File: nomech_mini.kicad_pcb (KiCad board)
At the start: 2 copper layers, 80 x 100 mm, 140 parts, among them CON1 USB_2B, CON2 AVR-ISP-6, P2 CONN_1, P3 CONN_1, P4 CONN_1, P5 CONN_1, P6 CONN_1, Q1 MOSFET_N, Q2 MOSFET_N, Q3 MOSFET_N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

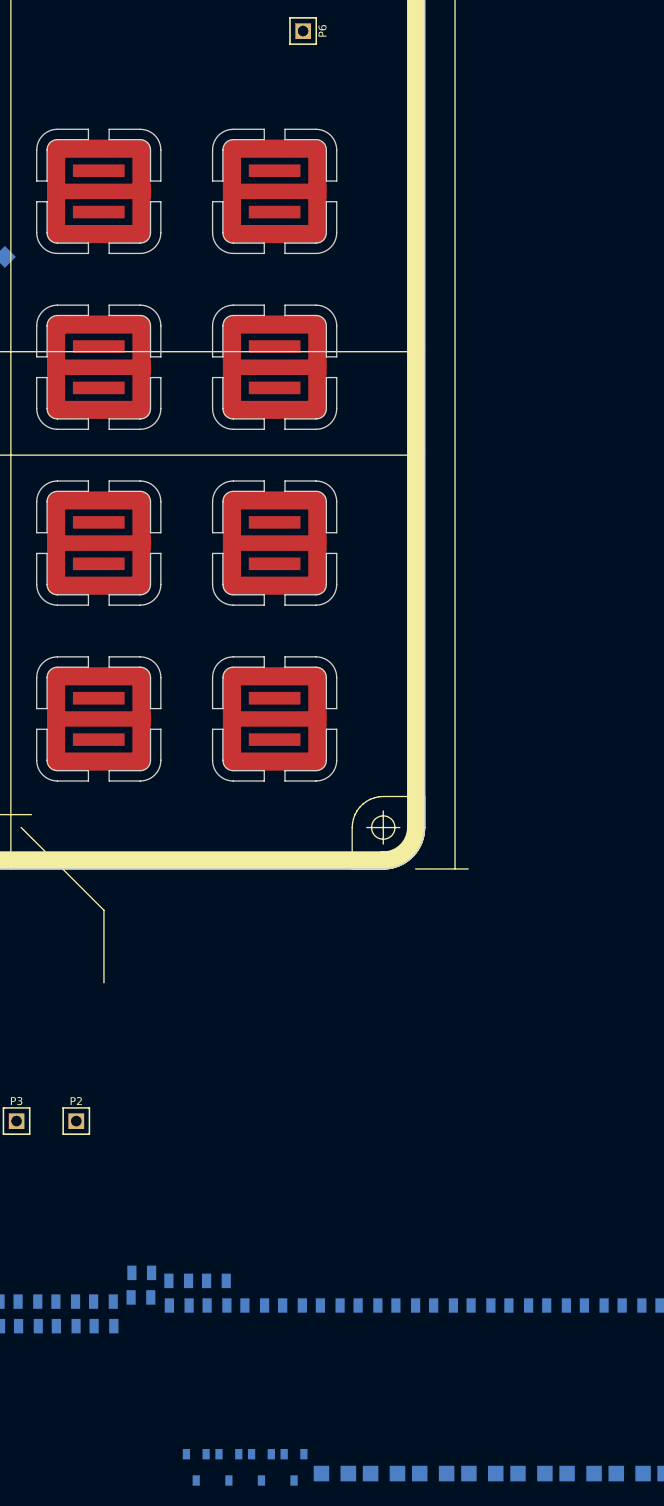
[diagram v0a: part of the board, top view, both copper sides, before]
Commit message: laying out LEDs
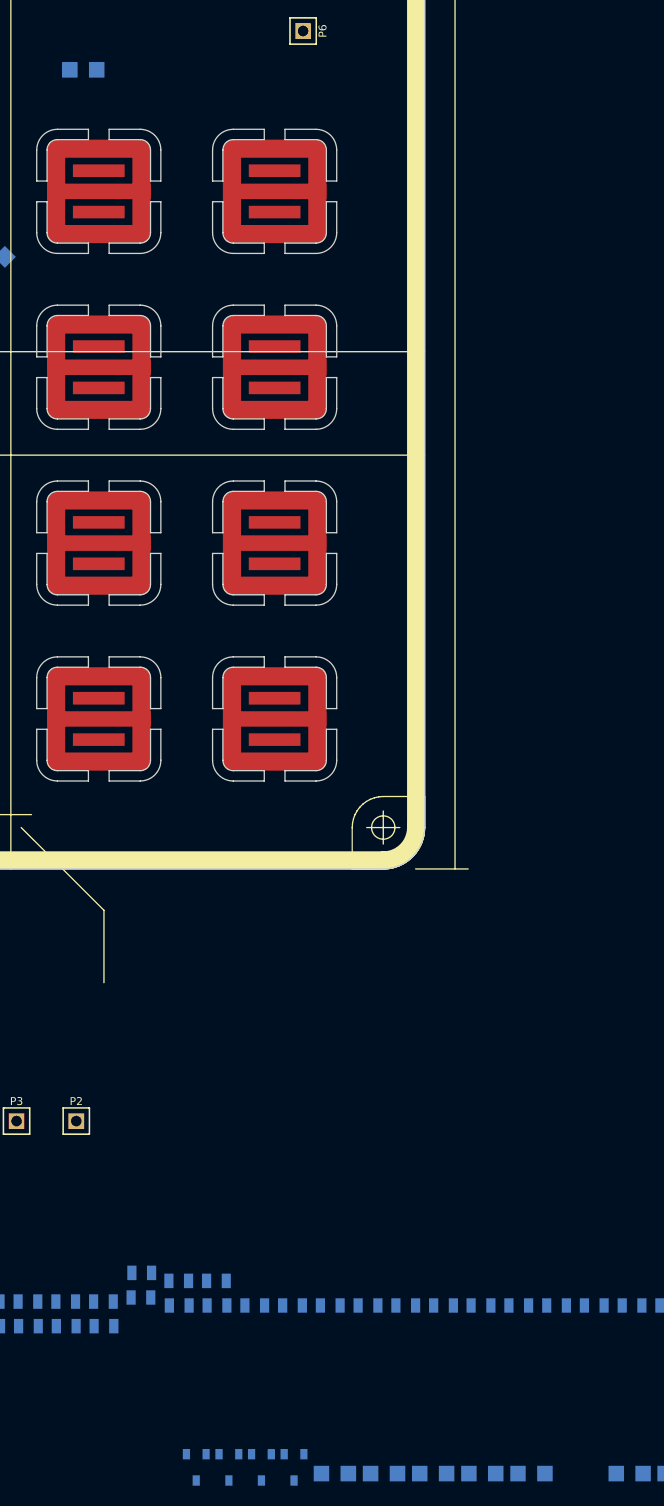
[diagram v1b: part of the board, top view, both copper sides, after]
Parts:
- moved D5 144.0 mm to (146.2, 106.5)
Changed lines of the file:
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@@
   )
   (module KPJA-2107SURCK (layer Back)
-    (at 194.325 242.2)
+    (at 146.25 106.5)
     (attr smd)
     (fp_text reference D5 (at 0.05 1.85) (layer B.SilkS)

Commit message: placing LEDS, working out laser cutting
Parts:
- moved D7 175.8 mm to (157.8, 111.2), turned to 45 degrees
- moved D9 173.1 mm to (106.8, 128.2), turned to 45 degrees
- moved R27 163.2 mm to (122.8, 115.8), turned to 90 degrees
- moved D33 160.8 mm to (147.2, 93.5)
- moved D19 160.2 mm to (123.8, 145.2), turned to 45 degrees
- moved R28 159.4 mm to (133.2, 126.2)
- moved D15 156.8 mm to (157.8, 128.2), turned to 45 degrees
- moved R25 154.8 mm to (105.8, 115.2), turned to 90 degrees
- moved D6 154.7 mm to (154.8, 125.2), turned to 225 degrees
- moved D25 137.0 mm to (106.8, 162.2), turned to 45 degrees
- moved D22 134.6 mm to (154.8, 159.2), turned to 225 degrees
- moved D23 131.5 mm to (157.8, 145.2), turned to 45 degrees
- moved D13 128.0 mm to (140.8, 128.2), turned to 45 degrees
- moved D14 123.7 mm to (154.8, 142.2), turned to 225 degrees
- moved R31 120.9 mm to (156.8, 115.8), turned to 90 degrees
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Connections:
- D1 pad 1: N-0000019 -> N-0000053
- D1 pad 2: GND -> LED_ROW_1_SW
- D10 pad 1: N-0000054 -> N-0000078
- D10 pad 2: LED_ROW_1_SW -> LED_ROW_2_SW
- D12 pad 1: N-0000070 -> N-0000086
- D12 pad 2: LED_ROW_3_SW -> LED_ROW_2_SW
- D13 pad 1: N-0000062 -> N-0000067
- D13 pad 2: LED_ROW_4_SW -> LED_ROW_2_SW
- D14 pad 1: N-0000081 -> N-0000087
- D14 pad 2: LED_ROW_1_SW -> LED_ROW_2_SW
- D15 pad 1: N-0000086 -> N-0000066
- D16 pad 1: N-0000083 -> N-0000085
- D16 pad 2: LED_ROW_3_SW -> LED_ROW_2_SW
- D17 pad 1: N-0000075 -> N-0000065
- D17 pad 2: LED_ROW_4_SW -> LED_ROW_3_SW
- D18 pad 1: N-0000051 -> N-0000084
- D18 pad 2: LED_ROW_1_SW -> LED_ROW_3_SW
- D19 pad 1: N-0000067 -> N-0000070
- D19 pad 2: LED_ROW_2_SW -> LED_ROW_3_SW
- D2 pad 1: N-0000053 -> N-0000074
- D20 pad 1: N-0000069 -> N-0000083
- D21 pad 1: N-0000061 -> N-0000069
- D21 pad 2: LED_ROW_4_SW -> LED_ROW_3_SW
- D22 pad 1: N-0000080 -> N-0000082
- D22 pad 2: LED_ROW_1_SW -> LED_ROW_3_SW
- D23 pad 1: N-0000087 -> N-0000068
- D23 pad 2: LED_ROW_2_SW -> LED_ROW_3_SW
- D24 pad 1: N-0000082 -> N-0000077
- D25 pad 1: N-0000073 -> N-0000063
- D26 pad 1: N-0000052 -> N-0000076
- D26 pad 2: LED_ROW_1_SW -> LED_ROW_4_SW
- D27 pad 1: N-0000066 -> N-0000062
- D27 pad 2: LED_ROW_2_SW -> LED_ROW_4_SW
- D28 pad 1: N-0000068 -> N-0000075
- D28 pad 2: LED_ROW_3_SW -> LED_ROW_4_SW
- D29 pad 1: N-0000064 -> N-0000061
- D3 pad 1: N-0000055 -> N-0000054
- D3 pad 2: LED_ROW_2_SW -> LED_ROW_1_SW
- D30 pad 1: N-0000079 -> N-0000073
- D30 pad 2: LED_ROW_1_SW -> LED_ROW_4_SW
- D31 pad 1: N-0000085 -> N-0000064
- D31 pad 2: LED_ROW_2_SW -> LED_ROW_4_SW
- D32 pad 1: N-0000077 -> N-0000072
- D32 pad 2: LED_ROW_3_SW -> LED_ROW_4_SW
- D33 pad 1: N-0000072 -> N-0000019
- D33 pad 2: LED_ROW_4_SW -> GND
- D4 pad 1: N-0000065 -> N-0000081
- D4 pad 2: LED_ROW_3_SW -> LED_ROW_1_SW
- D5 pad 1: N-0000063 -> N-0000051
- D5 pad 2: LED_ROW_4_SW -> LED_ROW_1_SW
- D6 pad 1: N-0000074 -> N-0000080
- D7 pad 1: N-0000078 -> N-0000052
- D7 pad 2: LED_ROW_2_SW -> LED_ROW_1_SW
- D8 pad 1: N-0000084 -> N-0000079
- D8 pad 2: LED_ROW_3_SW -> LED_ROW_1_SW
- D9 pad 1: N-0000076 -> N-0000055
- D9 pad 2: LED_ROW_4_SW -> LED_ROW_2_SW
- R26 pad 2: N-0000055 -> N-0000074
- R27 pad 1: LED_COLUMN_1 -> LED_COLUMN_2
- R27 pad 2: N-0000065 -> N-0000054
- R28 pad 1: LED_COLUMN_1 -> LED_COLUMN_2
- R28 pad 2: N-0000063 -> N-0000081
- R29 pad 1: LED_COLUMN_1 -> LED_COLUMN_3
- R29 pad 2: N-0000074 -> N-0000051
- R30 pad 1: LED_COLUMN_1 -> LED_COLUMN_3
- R30 pad 2: N-0000078 -> N-0000080
- R31 pad 1: LED_COLUMN_1 -> LED_COLUMN_4
- R31 pad 2: N-0000084 -> N-0000052
- R32 pad 1: LED_COLUMN_1 -> LED_COLUMN_4
- R32 pad 2: N-0000076 -> N-0000079
- R33 pad 1: LED_COLUMN_2 -> LED_COLUMN_1
- R33 pad 2: N-0000054 -> N-0000055
- R34 pad 1: LED_COLUMN_2 -> LED_COLUMN_1
- R34 pad 2: N-0000056 -> N-0000078
- R35 pad 2: N-0000070 -> N-0000056
- R36 pad 2: N-0000062 -> N-0000086
- R37 pad 1: LED_COLUMN_2 -> LED_COLUMN_3
- R37 pad 2: N-0000081 -> N-0000067
- R38 pad 1: LED_COLUMN_2 -> LED_COLUMN_3
- R38 pad 2: N-0000086 -> N-0000087
- R39 pad 1: LED_COLUMN_2 -> LED_COLUMN_4
- R39 pad 2: N-0000083 -> N-0000066
- R40 pad 1: LED_COLUMN_2 -> LED_COLUMN_4
- R40 pad 2: N-0000075 -> N-0000085
- R41 pad 1: LED_COLUMN_3 -> LED_COLUMN_1
- R41 pad 2: N-0000051 -> N-0000065
- R42 pad 1: LED_COLUMN_3 -> LED_COLUMN_1
- R42 pad 2: N-0000067 -> N-0000084
- R43 pad 1: LED_COLUMN_3 -> LED_COLUMN_2
- R43 pad 2: N-0000069 -> N-0000070
- R44 pad 1: LED_COLUMN_3 -> LED_COLUMN_2
- R44 pad 2: N-0000061 -> N-0000083
- R45 pad 2: N-0000080 -> N-0000069
- R46 pad 2: N-0000087 -> N-0000082
- R47 pad 1: LED_COLUMN_3 -> LED_COLUMN_4
- R47 pad 2: N-0000082 -> N-0000068
- R48 pad 1: LED_COLUMN_3 -> LED_COLUMN_4
- R48 pad 2: N-0000073 -> N-0000077
- R49 pad 1: LED_COLUMN_4 -> LED_COLUMN_1
- R49 pad 2: N-0000052 -> N-0000063
- R50 pad 1: LED_COLUMN_4 -> LED_COLUMN_1
- R50 pad 2: N-0000066 -> N-0000076
- R51 pad 1: LED_COLUMN_4 -> LED_COLUMN_2
- R51 pad 2: N-0000068 -> N-0000062
- R52 pad 1: LED_COLUMN_4 -> LED_COLUMN_2
- R52 pad 2: N-0000064 -> N-0000075
- R53 pad 1: LED_COLUMN_4 -> LED_COLUMN_3
- R53 pad 2: N-0000079 -> N-0000061
- R54 pad 1: LED_COLUMN_4 -> LED_COLUMN_3
- R54 pad 2: N-0000085 -> N-0000073
- R55 pad 2: N-0000077 -> N-0000064
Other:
- board size 80 x 100 mm -> 130.7 x 63 mm

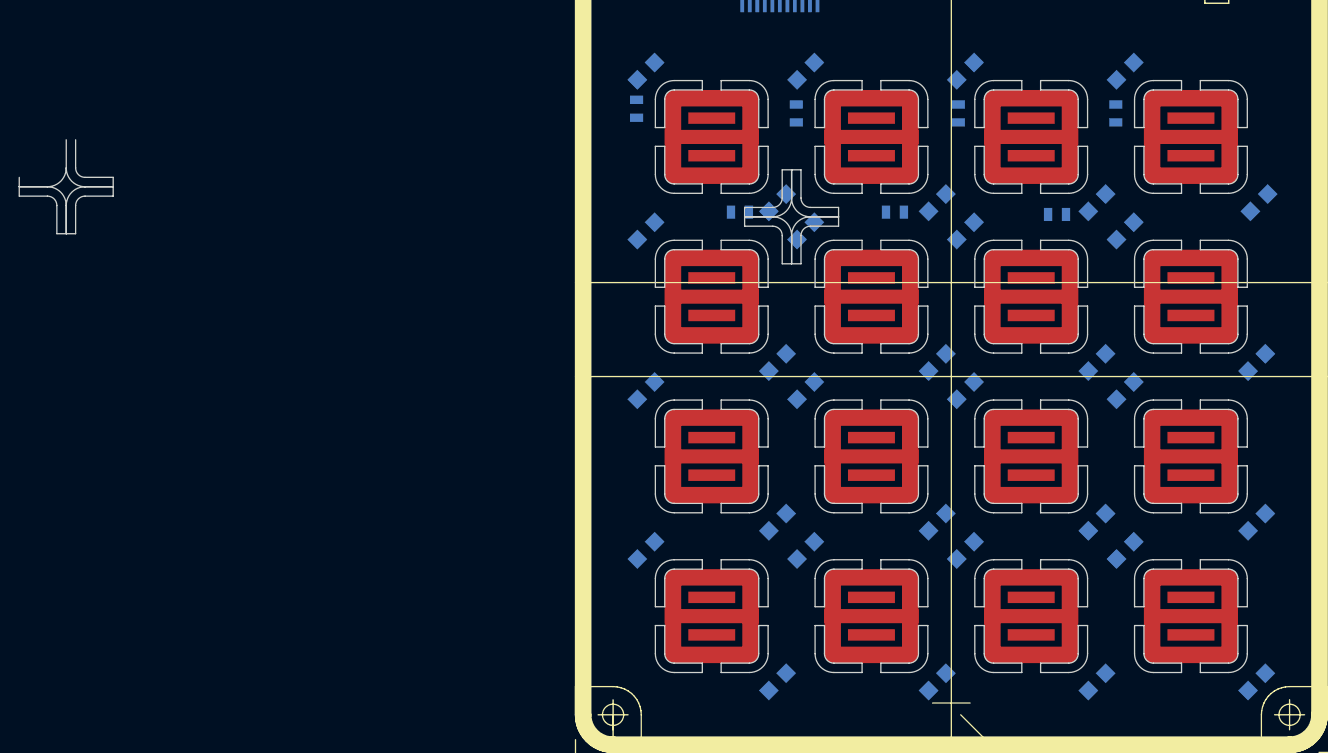
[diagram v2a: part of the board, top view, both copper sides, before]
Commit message: messing about with edge-cuts, putting them in .mod
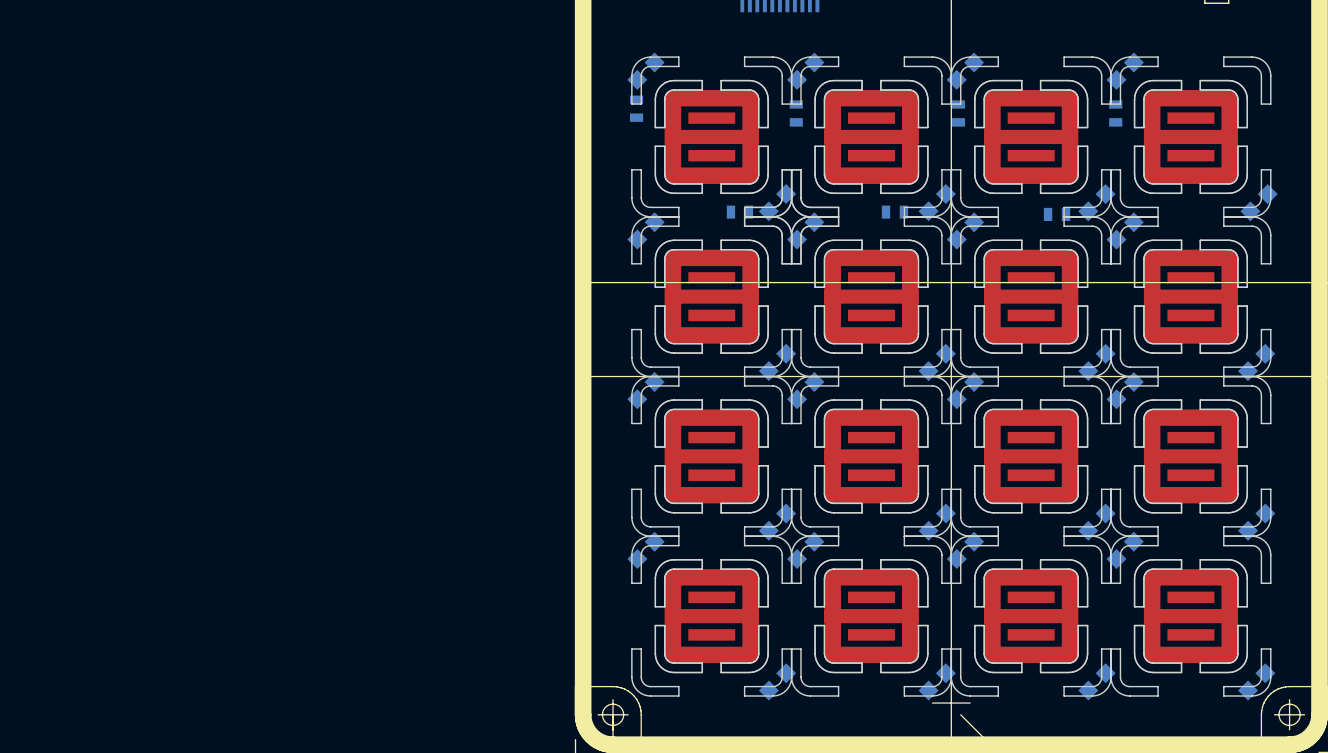
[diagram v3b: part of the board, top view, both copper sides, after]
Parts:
- E1, E10, E11, E12, E13, E14, E15, E16, E2, E3, E4, E5, E6, E7, E8, E9: footprint cap-electrode_10mm_2layer -> cap-electrode_10mm_2layer_cutout
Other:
- board size 130.7 x 63 mm -> 63 x 63 mm

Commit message: doing cutouts in the electrode module
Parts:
- E1, E10, E11, E12, E13, E14, E15, E16, E2, E3, E4, E5, E6, E7, E8, E9: footprint cap-electrode_10mm_2layer_cutout -> cap-electrode_10mm_2layer_cutout3
- moved D8 0.25 mm to (171.8, 125.2)

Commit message: most Rs placed
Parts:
- moved R49 170.7 mm to (110.8, 160.8), turned to 180 degrees
- moved R35 154.8 mm to (127.8, 126.8), turned to 180 degrees
- moved R36 151.8 mm to (133.7, 143.8)
- moved C8 150.3 mm to (129.3, 90.0), turned to 270 degrees
- moved R1 149.4 mm to (164.1, 92.0)
- moved C3 149.1 mm to (117.5, 89.3), turned to 180 degrees
- moved R43 147.6 mm to (127.8, 143.8), turned to 180 degrees
- moved R44 146.6 mm to (133.7, 160.8)
- moved C1 146.3 mm to (131.9, 90.6), turned to 270 degrees
- moved R33 145.7 mm to (110.8, 126.8), turned to 180 degrees
- moved R2 145.0 mm to (135.4, 92.0), turned to 180 degrees
- moved R52 143.5 mm to (139.2, 172.2), turned to 270 degrees
- moved R51 142.0 mm to (127.8, 160.8), turned to 180 degrees
- moved R34 141.7 mm to (116.7, 143.8)
- moved R3 141.7 mm to (135.4, 94.1), turned to 180 degrees
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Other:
- board size 63 x 63 mm -> 185.6 x 63 mm

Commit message: placed?
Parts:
- removed 80x80: 80mm, dp_pcb-DP8080_V1_drawing
- removed C3, C5: 100nF, SM0805
- removed C6, C8: 10nF, SM0805
- moved R19 169.4 mm to (111.8, 99.8), turned to 180 degrees
- moved P3 167.9 mm to (126.6, 40.7)
- moved P4 167.9 mm to (120.8, 40.7)
- moved P2 167.9 mm to (132.4, 40.7)
- moved P5 167.9 mm to (115.0, 40.7)
- moved C16 155.2 mm to (136.1, 101.2)
- moved R21 150.8 mm to (124.5, 101.9), turned to 180 degrees
- moved R17 150.5 mm to (124.5, 99.8), turned to 180 degrees
- moved R22 149.1 mm to (120.2, 101.9), turned to 180 degrees
- moved R18 148.9 mm to (120.2, 99.8), turned to 180 degrees
- moved R24 147.5 mm to (115.9, 101.9), turned to 180 degrees
- moved R20 147.3 mm to (115.9, 99.8), turned to 180 degrees
- moved R23 145.8 mm to (111.8, 101.9), turned to 180 degrees
- moved Q3 143.8 mm to (111.8, 105.2)
- moved Q4 143.5 mm to (115.8, 105.2)
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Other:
- board size 185.6 x 63 mm -> 63 x 63 mm

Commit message: starting routing...
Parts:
- E1, E10, E11, E12, E13, E14, E15, E16, E2, E3, E4, E5, E6, E7, E8, E9: footprint cap-electrode_10mm_2layer_cutout3 -> cap-electrode_10mm_2layer_cutout4
- moved L2 73.1 mm to (217.0, 52.2)
- moved C11 73.1 mm to (204.3, 36.4)
- moved C12 73.1 mm to (222.1, 47.6)
- moved C4 73.1 mm to (208.4, 36.4)
- moved C7 73.1 mm to (197.0, 42.2)
- moved C9 73.1 mm to (222.1, 41.5)
- moved CON1 73.1 mm to (189.7, 32.0)
- moved CON2 73.1 mm to (170.5, 42.2)
- moved L1 73.1 mm to (194.7, 40.2)
- moved R1 73.1 mm to (170.6, 38.5)
- moved R2 73.1 mm to (200.0, 36.7)
- moved R3 73.1 mm to (200.0, 38.8)
- moved R4 73.1 mm to (175.8, 38.5)
- moved X1 73.1 mm to (218.5, 44.5)
- moved C1 73.1 mm to (197.2, 49.2)
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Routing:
- net LED_ROW_1_SW: track 0.00 -> 134.3 mm
- net Y4: track 0.00 -> 85.0 mm, vias 0 -> 8
- net Y1: track 0.00 -> 84.4 mm, vias 0 -> 9
- net LED_COLUMN_1: track 0.00 -> 75.5 mm
- net Y2: track 0.00 -> 70.2 mm, vias 0 -> 8
- net Y3: track 0.00 -> 70.2 mm, vias 0 -> 8
- net X2: track 0.00 -> 53.0 mm, vias 0 -> 1
- net X1: track 0.00 -> 53.0 mm, vias 0 -> 1
- net X3: track 0.00 -> 53.0 mm, vias 0 -> 1
- net X4: track 0.00 -> 44.8 mm, vias 0 -> 1
- net N-0000054: track 0.00 -> 16.6 mm
- net N-0000053: track 0.00 -> 16.2 mm
- net LED_COLUMN_2: track 0.00 -> 14.4 mm
- net LED_ROW_2_SW: track 0.00 -> 12.6 mm
- net N-0000076: track 0.00 -> 6.14 mm
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
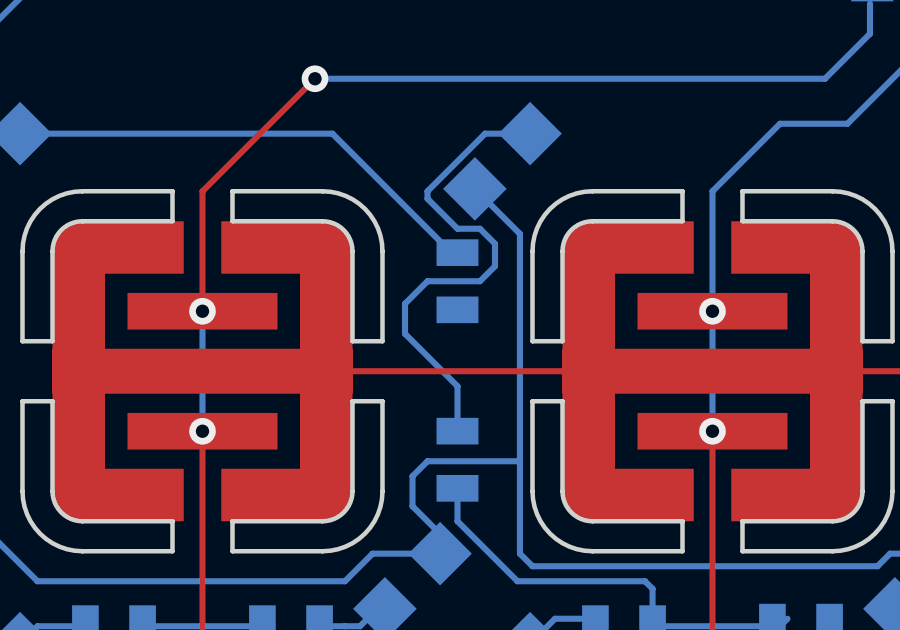
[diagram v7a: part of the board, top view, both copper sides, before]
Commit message: changing electrode
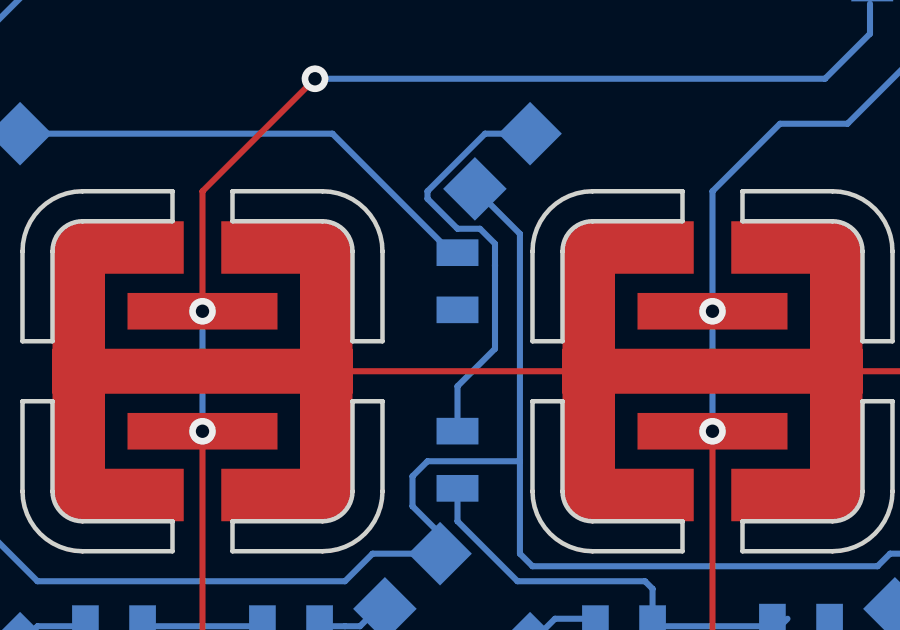
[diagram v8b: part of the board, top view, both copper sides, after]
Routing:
- net N-0000054: track 16.6 -> 14.2 mm
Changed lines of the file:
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@@
     (thickness 1.6002)
     (drawings 602)
-    (tracks 231)
+    (tracks 229)
     (zones 0)
     (modules 135)
@@
     (pad_to_mask_clearance 0.254)
     (aux_axis_origin 0 0)
-    (visible_elements 7FFFFFFF)
+    (visible_elements 7FFFF7FF)
     (pcbplotparams
       (layerselection 71073793)
@@
   (segment (start 118.080761 110.330761) (end 107.669239 110.330761) (width 0.2032) (layer Back) (net 44))
   (segment (start 122.0475 114.2975) (end 118.080761 110.330761) (width 0.2032) (layer Back) (net 44))
-  (segment (start 120.5 117) (end 122.25 118.75) (width 0.2032) (layer Back) (net 45))
-  (segment (start 123.5 114) (end 123.5 114.75) (width 0.2032) (layer Back) (net 45))
-  (segment (start 124.669239 110.330761) (end 123.169239 110.330761) (width 0.2032) (layer Back) (net 45))
+  (segment (start 123.5 114.7) (end 123.5 117.5) (width 0.2032) (layer Back) (net 45))
   (segment (start 122.25 118.75) (end 122.25 120.2475) (width 0.2032) (layer Back) (net 45))
-  (segment (start 120.5 116) (end 120.5 117) (width 0.2032) (layer Back) (net 45))
-  (segment (start 121.25 115.25) (end 120.5 116) (width 0.2032) (layer Back) (net 45))
-  (segment (start 123 115.25) (end 121.25 115.25) (width 0.2032) (layer Back) (net 45))
-  (segment (start 123.5 114.75) (end 123 115.25) (width 0.2032) (layer Back) (net 45))
+  (segment (start 123.5 117.5) (end 122.25 118.75) (width 0.2032) (layer Back) (net 45))
+  (segment (start 123.5 114) (end 123.5 114.7) (width 0.2032) (layer Back) (net 45))
+  (segment (start 123.5 114.7) (end 123.5 114.75) (width 0.2032) (layer Back) (net 45))
+  (segment (start 124.669239 110.330761) (end 123.169239 110.330761) (width 0.2032) (layer Back) (net 45))
   (segment (start 123 113.5) (end 123.5 114) (width 0.2032) (layer Back) (net 45))
   (segment (start 122.25 113.5) (end 123 113.5) (width 0.2032) (layer Back) (net 45))
